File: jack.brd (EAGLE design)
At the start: 100 x 80 mm, 28 parts, among them IC1 NUF2221W1T2G, IC2 ATSAMD21G18, IC3 LDO, SW1 SPST, X1 TSX-3225 24.0000MF10Z-C3

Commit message: :octocat: Moved a few components on layout
Started layout process.... I'm going really slow (work is a pain)
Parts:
- moved R1 55.4 mm to (8.38, 15.2), turned to 90 degrees
- moved IC3 47.4 mm to (7.62, 10.4), turned to 90 degrees
- moved IC1 35.8 mm to (7.62, 19.1), turned to 180 degrees
- moved L2 35.4 mm to (14.0, 38.1), turned to 90 degrees
- moved J1 33.0 mm to (3.81, 19.1), turned to 270 degrees
- moved C8 29.6 mm to (6.35, 15.2), turned to 90 degrees
- moved IC2 26.9 mm to (26.7, 15.2), turned to 45 degrees
- moved JP1 21.6 mm to (27.9, 1.27)
- moved JP2 1.27 mm to (27.9, 29.2), turned to 180 degrees

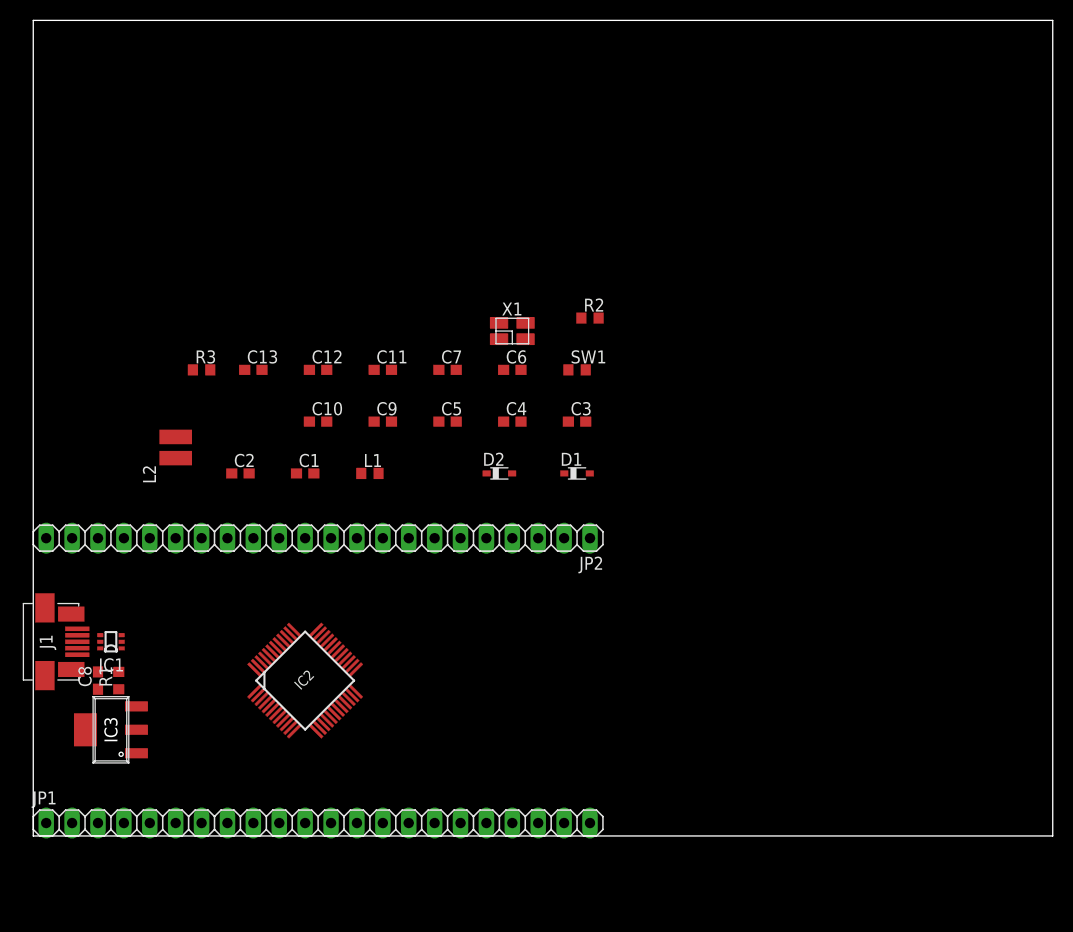
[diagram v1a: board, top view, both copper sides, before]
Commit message: :hatching_chick: Polished schematic, started layout
I polished the schematic so to let people easily understand what does
what, dividing it in sections with a description; I did a hi-res picture
of it so to see it without having to open Eagle CAD; also, I started the
layout process; you can already see on the PCB where stuff should go in
the end
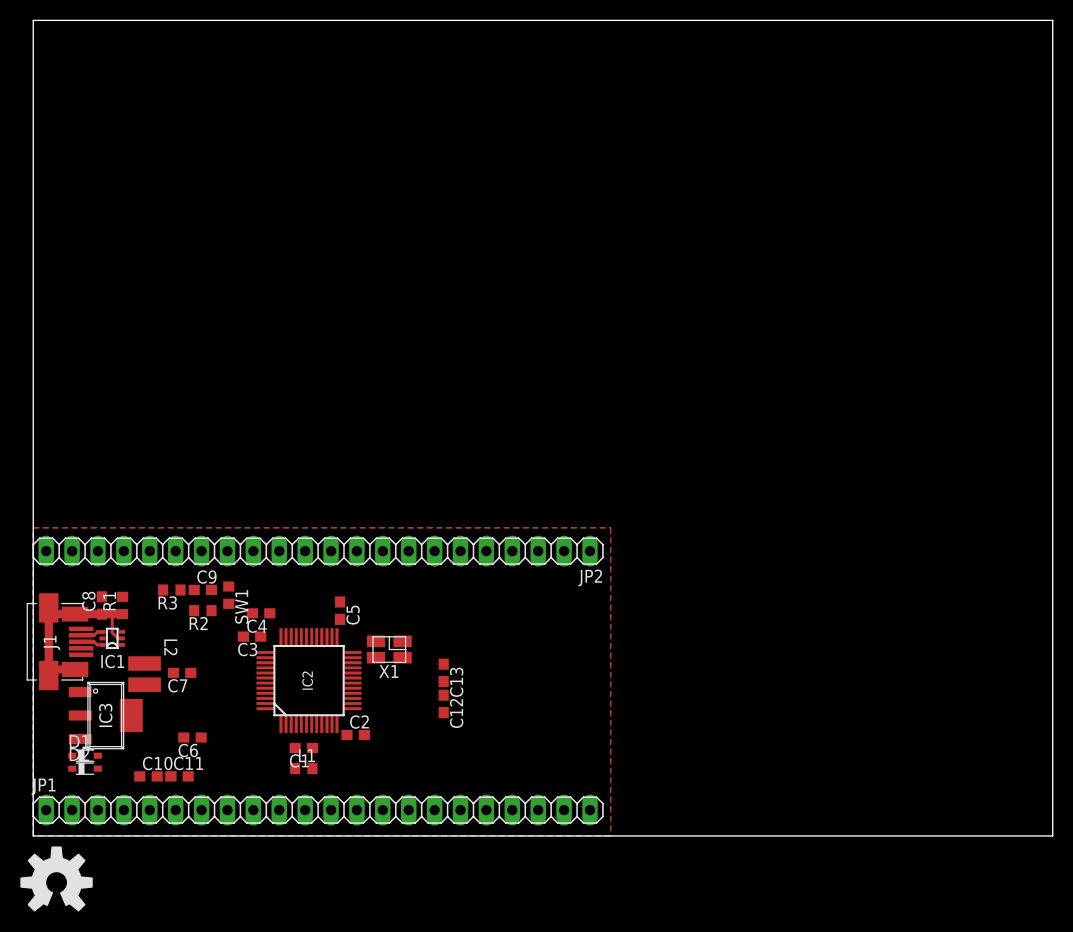
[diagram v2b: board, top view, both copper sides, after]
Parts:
- added LOGO1: OSHW-LOGOL, SparkFun-Aesthetics:OSHW-LOGO-L
- moved D1 55.6 mm to (5.08, 7.87)
- moved D2 49.9 mm to (5.08, 6.60)
- moved C6 47.8 mm to (15.6, 9.65), turned to 180 degrees
- moved R2 47.6 mm to (16.6, 22.1), turned to 180 degrees
- moved C11 44.6 mm to (14.4, 5.84)
- moved SW1 40.7 mm to (19.2, 23.6), turned to 270 degrees
- moved C7 39.5 mm to (14.6, 16.0), turned to 180 degrees
- moved C10 38.6 mm to (11.3, 5.84)
- moved C3 38.2 mm to (21.5, 19.6), turned to 180 degrees
- moved C13 35.1 mm to (40.3, 16.0), turned to 270 degrees
- moved C12 35.0 mm to (40.3, 13.0), turned to 270 degrees
- moved X1 33.5 mm to (34.9, 18.3), turned to 180 degrees
- moved C4 31.0 mm to (22.4, 21.8), turned to 180 degrees
- moved L1 29.7 mm to (26.5, 6.60)
- moved C2 28.0 mm to (31.6, 9.91)
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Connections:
- removed net 40: JP2.14
- removed net AGND: C1.2, C6.2, IC2.5
- net !RESET: now also JP2.12; no longer JP2.15
- net 25: now also JP2.1; no longer JP2.3
- net 26: now also JP2.2; no longer JP2.4
- net 27: now also JP2.3; no longer JP2.5
- net 28: now also JP2.4; no longer JP2.6
- net 29: now also JP2.5; no longer JP2.7
- net 30: now also JP2.6; no longer JP2.8
- net 31: now also JP2.7; no longer JP2.9
- net 32: now also JP2.8; no longer JP2.10
- net 37: now also JP2.9; no longer JP2.11
- net 38: now also JP2.10; no longer JP2.12
- net 39: now also JP2.11; no longer JP2.13
- net 41: now also JP2.13; no longer JP2.16
- net 45: now also JP2.14; no longer JP2.17
- net 46: now also JP2.15; no longer JP2.18
- net 47: now also JP2.16
- net 48: now also JP2.17
- net GNDANA: now also C1.2, C6.2, IC2.5
- net VBUS: now also JP2.21
- net VDD: now also JP2.19; no longer JP2.20
- net VDDF: now also JP2.18; no longer JP2.21
- net VIN: now also JP2.20; no longer JP2.19
- net XIN: no longer JP2.1
- net XOUT: no longer JP2.2
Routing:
- net SH_GND: track 0.00 -> 19.7 mm
- net D-IN: track 0.00 -> 2.23 mm
- net D+IN: track 0.00 -> 2.22 mm
- added copper zone on layer 1, net GND
- added copper zone on layer 16, net GND

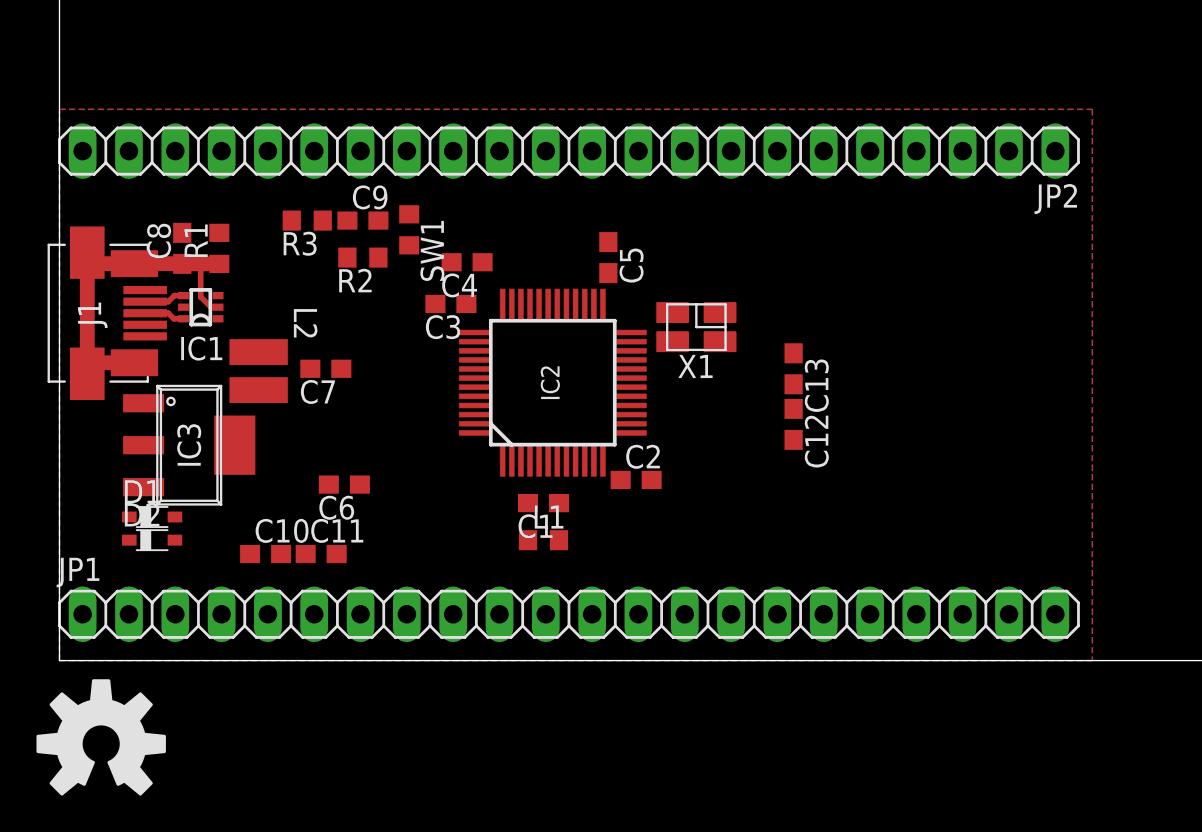
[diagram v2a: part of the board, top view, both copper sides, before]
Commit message: :wavy_dash: Progressing with layout
Still dealing with layout, in particular dealing with analog/digital
power, decoupling caps and correct power grounding (one ground to rule
them all, or local a/d planes near chip and then star ground near LDO?)
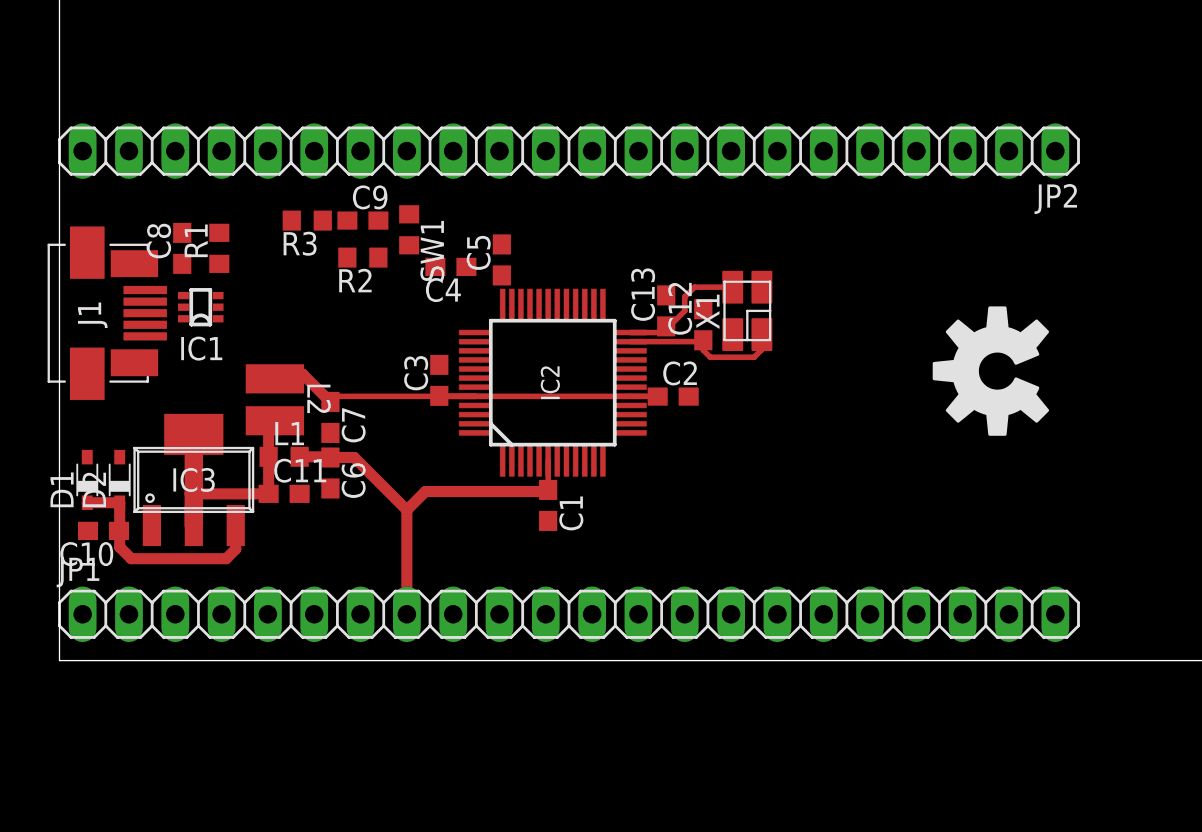
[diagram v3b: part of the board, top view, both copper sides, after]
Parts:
- moved LOGO1 53.2 mm to (51.4, 15.9), turned to 90 degrees
- moved L1 14.9 mm to (12.3, 11.2)
- moved C10 8.98 mm to (2.41, 7.11), turned to 180 degrees
- moved C13 7.67 mm to (33.3, 19.2), turned to 90 degrees
- moved C12 7.37 mm to (35.3, 18.4), turned to 90 degrees
- moved C5 5.84 mm to (24.3, 22.0), turned to 90 degrees
- moved C2 5.00 mm to (33.7, 14.5)
- moved C3 4.24 mm to (20.8, 15.4), turned to 90 degrees
- moved D1 4.10 mm to (1.52, 9.91), turned to 90 degrees
- moved C11 3.88 mm to (12.3, 9.14)
- moved D2 3.75 mm to (3.30, 9.91), turned to 90 degrees
- moved X1 2.93 mm to (37.7, 19.2), turned to 90 degrees
- moved C7 2.68 mm to (14.9, 13.3), turned to 270 degrees
- moved IC3 1.92 mm to (7.37, 9.91), turned to 0 degrees
- moved L2 1.76 mm to (11.8, 14.4)
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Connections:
- net N$2 renamed LDOIN
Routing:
- net VDDF: track 0.00 -> 24.8 mm
- net VDDANA: track 0.00 -> 22.7 mm
- net SH_GND: track 19.7 -> 0.00 mm
- net VDD: track 0.00 -> 14.4 mm
- net LDOIN: track 0.00 -> 12.4 mm
- net XIN: track 0.00 -> 8.95 mm
- net XOUT: track 0.00 -> 7.09 mm
- net D-IN: track 2.23 -> 0.00 mm
- net D+IN: track 2.22 -> 0.00 mm
- removed copper zone on layer 1, net GND
- removed copper zone on layer 16, net GND

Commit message: Minor changes
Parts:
- added JP3: SAM_ARM_JTAG, jack:2X5-SHROUDED
- moved C1 9.44 mm to (36.1, 6.73)
- moved LOGO1 8.28 mm to (43.2, 15.2)
- moved C3 3.99 mm to (17.4, 17.4), turned to 0 degrees
- moved J1 3.81 mm to (4.19, 15.2)
- moved IC1 3.81 mm to (7.75, 15.6)
- moved C2 2.80 mm to (36.4, 14.6)
- moved IC2 1.76 mm to (25.5, 14.4), turned to 135 degrees
- moved C6 1.69 mm to (16.5, 9.91)
- moved C7 1.69 mm to (16.5, 13.0)
- moved C10 1.69 mm to (4.06, 6.73)
- moved D2 1.69 mm to (4.95, 9.53)
- moved C11 1.69 mm to (14.0, 8.76)
- moved D1 1.69 mm to (3.17, 9.53)
- moved IC3 1.69 mm to (9.02, 9.53)
- moved L1 1.69 mm to (14.0, 10.8)
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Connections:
- new net N$1: JP3.1
- new net N$10: JP3.4
- new net N$11: JP3.2
- new net N$2: JP3.3
- new net N$4: JP3.5
- new net N$5: JP3.7
- new net N$6: JP3.9
- new net N$7: JP3.10
- new net N$8: JP3.8
- new net N$9: JP3.6
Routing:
- net VDDF: track 24.8 -> 0.00 mm
- net VDDANA: track 22.7 -> 1.71 mm
- net XIN: track 8.95 -> 0.00 mm
- net XOUT: track 7.09 -> 0.00 mm

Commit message: :satellite: Modified .gitignore, updated schematic, progressing layout
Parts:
- removed JP3: SAM_ARM_JTAG, jack:2X5-SHROUDED
- added R4: 0, rcl:R0603
- C1, C10, C12, C13, C2, C3, C4, C5, C9: device rcl:C0603 -> rcl:C0402K
- SW1: value SPST -> SPST3.5X6MM; device jack:0603 -> jack:SWITCH-SMD-3.5X6MM
- X1: device jack:TSX-3225 -> jack:CX-3225
- moved SW1 32.7 mm to (50.8, 15.2), turned to 90 degrees
- moved R3 32.5 mm to (46.0, 22.0), turned to 90 degrees
- moved R2 31.4 mm to (48.0, 22.0), turned to 90 degrees
- moved L2 29.0 mm to (42.4, 11.8), turned to 180 degrees
- moved C6 28.1 mm to (44.6, 8.76), turned to 0 degrees
- moved C11 27.6 mm to (41.5, 6.73)
- moved L1 27.6 mm to (41.5, 8.76)
- moved IC3 27.3 mm to (36.3, 9.02), turned to 270 degrees
- moved C10 27.1 mm to (31.1, 6.73)
- moved D1 27.1 mm to (30.2, 9.53)
- moved D2 27.1 mm to (32.0, 9.53)
- moved JP1 25.4 mm to (27.9, 27.9), turned to 180 degrees
- moved JP2 25.4 mm to (27.9, 2.54), turned to 0 degrees
- moved C7 22.6 mm to (39.1, 12.3)
- moved X1 19.2 mm to (19.1, 23.6), turned to 0 degrees
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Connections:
- net 45 renamed SWCLK
- net 46 renamed SWDIO
- removed net N$1: JP3.1
- removed net N$10: JP3.4
- removed net N$11: JP3.2
- removed net N$2: JP3.3
- removed net N$4: JP3.5
- removed net N$5: JP3.7
- removed net N$6: JP3.9
- removed net N$7: JP3.10
- removed net N$8: JP3.8
- removed net N$9: JP3.6
- net GND: now also R4.1
- net GNDANA: now also R4.2
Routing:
- net VDD: track 14.4 -> 0.00 mm
- net LDOIN: track 12.4 -> 0.00 mm
- net D-OUT: track 0.00 -> 9.83 mm
- net D+OUT: track 0.00 -> 9.80 mm
- net GND: track 0.00 -> 7.17 mm
- net VDDF: track 0.00 -> 6.76 mm
- net XIN: track 0.00 -> 6.23 mm
- net XOUT: track 0.00 -> 6.04 mm
- net D+IN: track 0.00 -> 3.76 mm
- net D-IN: track 0.00 -> 3.75 mm
- net !RESET: track 0.00 -> 2.69 mm
- net VDDCORE: track 0.00 -> 2.35 mm
- net GNDANA: track 0.00 -> 1.61 mm
- added copper zone on layer 1, net GND
- added copper zone on layer 16, net GND

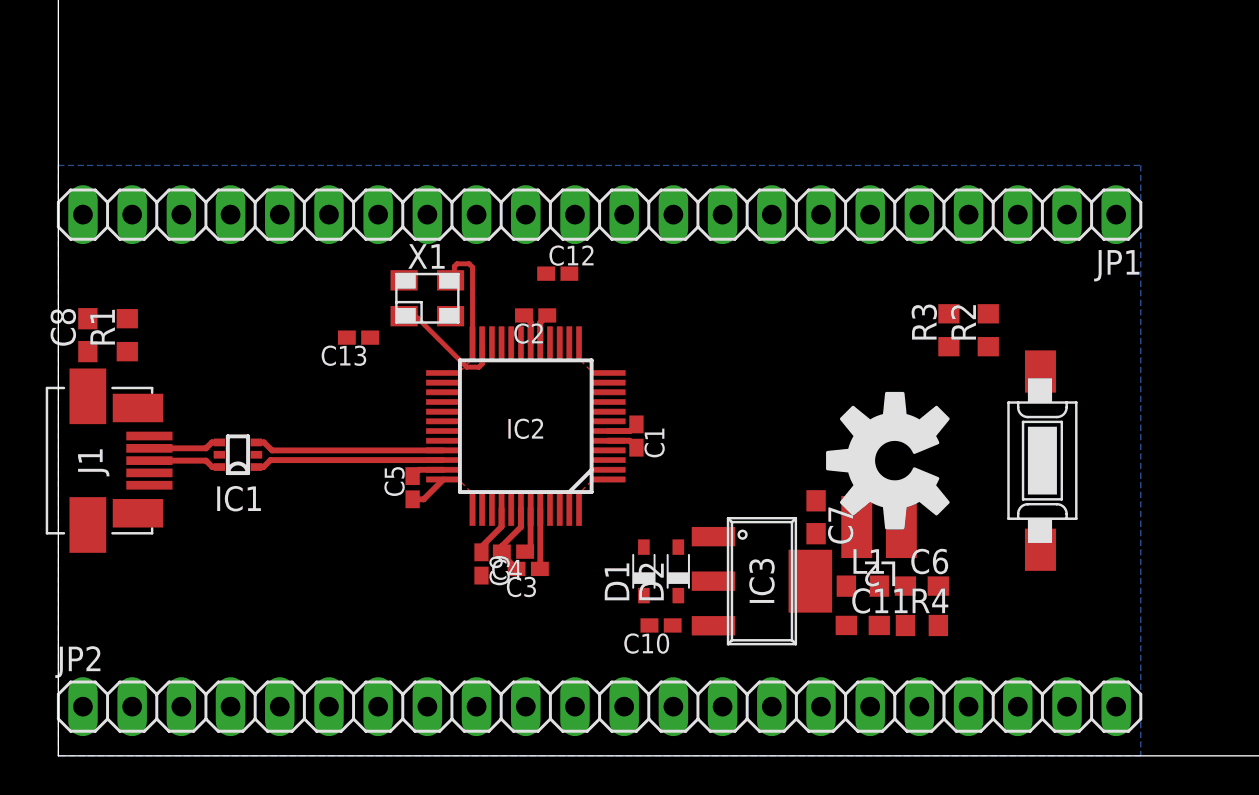
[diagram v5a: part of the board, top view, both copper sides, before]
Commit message: :paperclip: Ultimating critical parts layout
Finishing crystal, decoupling caps and USB signals an parts layout;
trying to figure out where to move the rest...
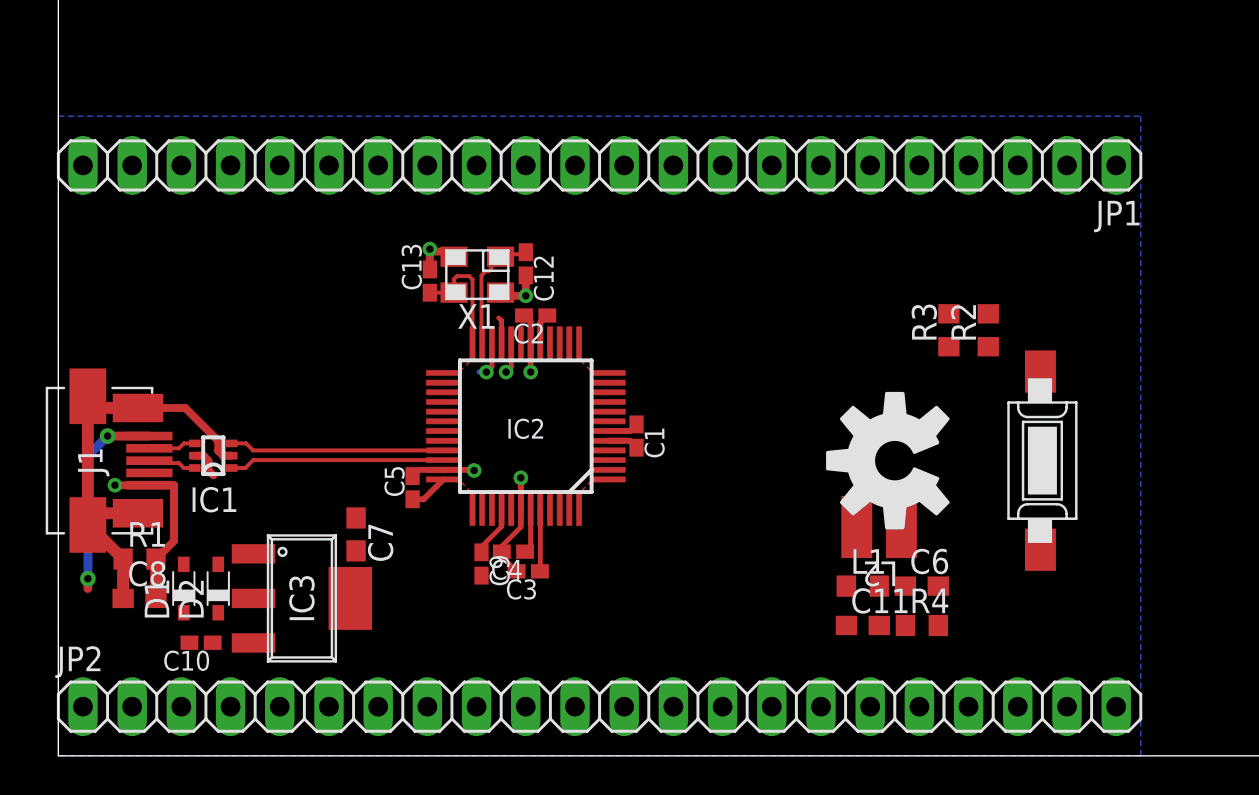
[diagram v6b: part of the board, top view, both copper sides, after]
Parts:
- moved IC3 23.8 mm to (12.6, 8.13)
- moved C10 23.8 mm to (7.37, 5.84)
- moved C7 23.8 mm to (15.4, 11.4)
- moved D1 23.8 mm to (6.48, 8.64)
- moved D2 23.8 mm to (8.26, 8.64)
- moved C8 13.8 mm to (4.19, 8.13), turned to 0 degrees
- moved R1 11.6 mm to (4.19, 10.2), turned to 0 degrees
- moved C13 4.70 mm to (19.2, 24.5), turned to 90 degrees
- moved X1 2.85 mm to (21.6, 24.8), turned to 180 degrees
- moved JP1 2.54 mm to (27.9, 30.5)
- moved C12 1.73 mm to (24.1, 25.4), turned to 270 degrees
- moved IC1 1.27 mm to (8.00, 15.5)
- moved C3 0.13 mm to (24.3, 9.53)
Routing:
- net SH_GND: track 0.00 -> 22.5 mm
- net GND: track 7.17 -> 26.3 mm, vias 0 -> 6
- net VBUS: track 0.00 -> 10.5 mm, vias 0 -> 2
- net 22: track 0.00 -> 1.95 mm, vias 0 -> 1
- net VDD: track 0.00 -> 1.67 mm
- net 20: track 0.00 -> 1.57 mm, vias 0 -> 1
- net 21: track 0.00 -> 1.40 mm
- net D-IN: track 3.75 -> 2.45 mm
- net D+OUT: track 9.80 -> 11.1 mm
- net D+IN: track 3.76 -> 2.51 mm
- net D-OUT: track 9.83 -> 11.1 mm
